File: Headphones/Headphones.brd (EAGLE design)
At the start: 50 x 50 mm, 3 parts, among them U1 SI4468

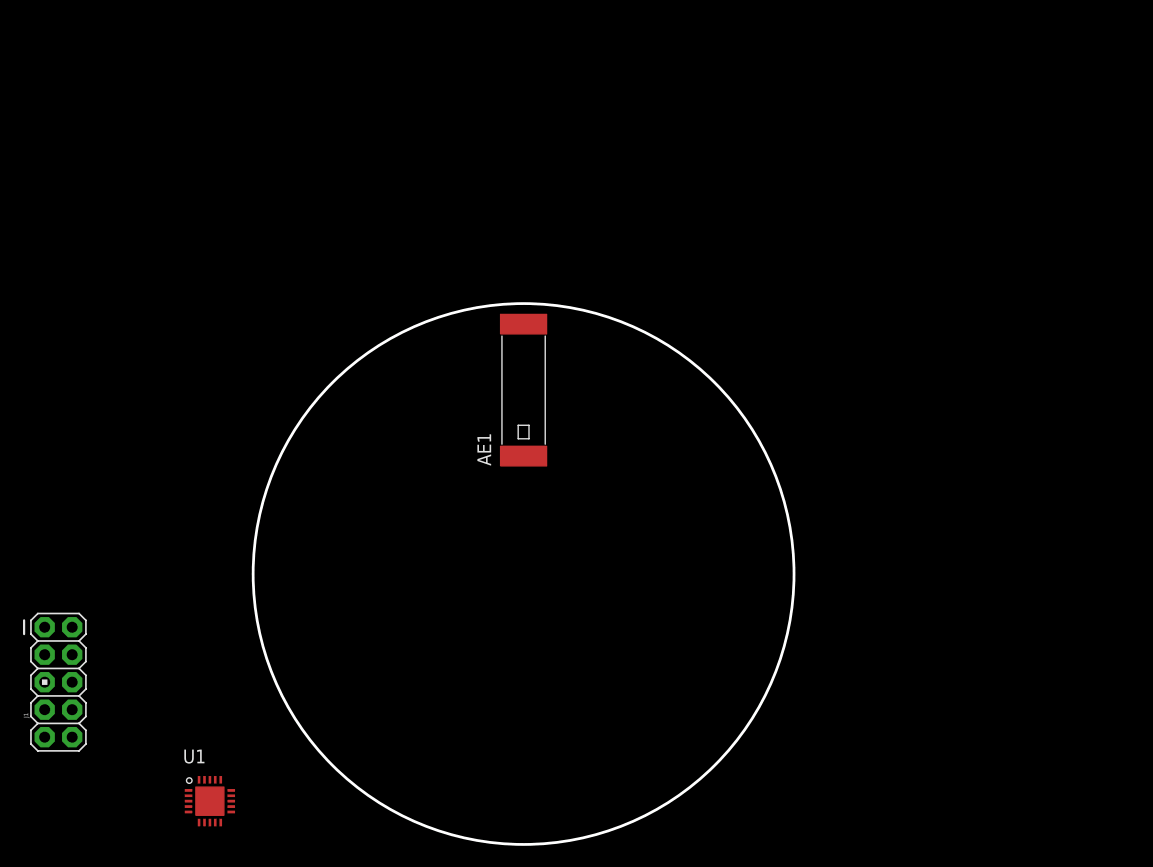
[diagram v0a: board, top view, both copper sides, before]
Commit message: Component placement is mostly complete. Need to finish routing
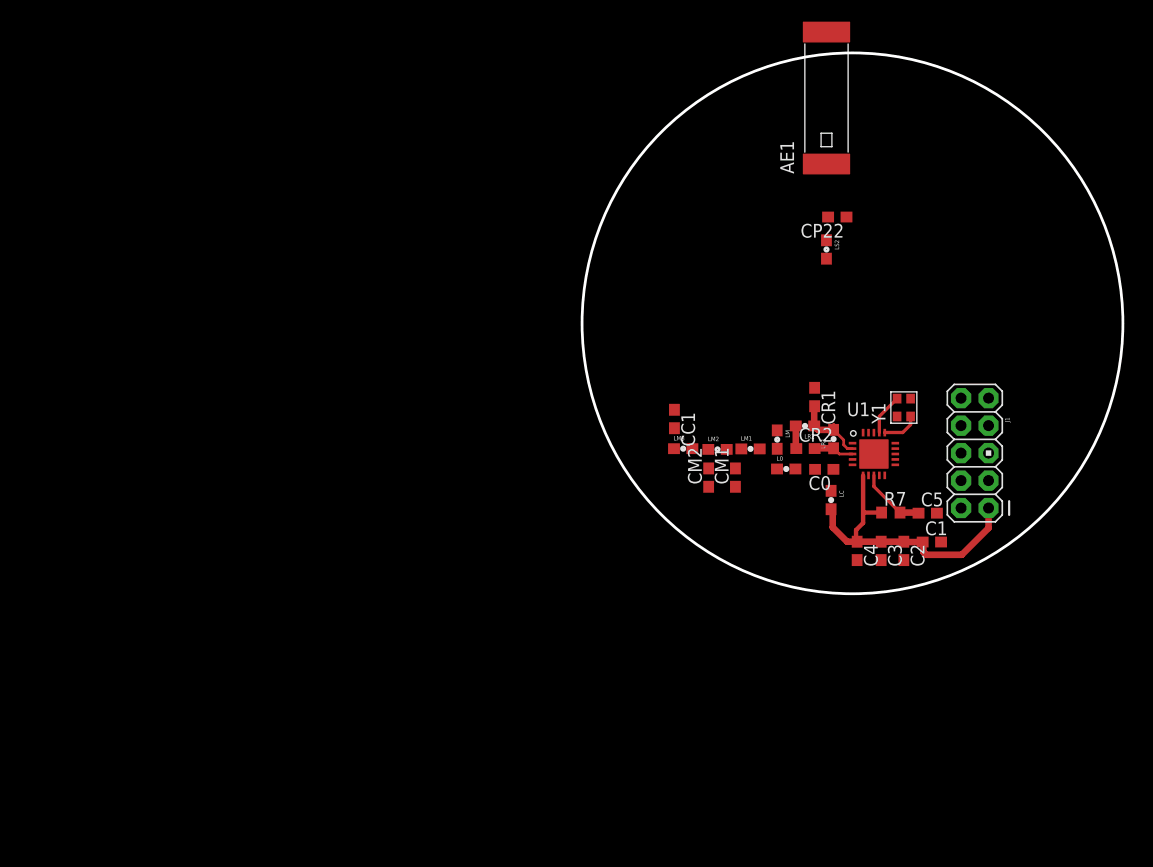
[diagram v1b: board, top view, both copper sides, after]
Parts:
- added C0, CM1, CM2: 4.7pF, resistor:C0603
- added C1: 2.2uF, resistor:C0603
- added C2, C5: 100nF, resistor:C0603
- added C3: 100pF, resistor:C0603
- added C4: 220pF, resistor:C0603
- added CC1: 56pF, resistor:C0603
- added CP22: 1.2pF, resistor:C0603
- added CR1: 3pF, resistor:C0603
- added CR2: 1pF, resistor:C0603
- added L0: 3.3nH, SparkFun-Passives:0603
- added LC: 100nH, SparkFun-Passives:0603
- added LM: 6.2nH, SparkFun-Passives:0603
- added LM1, LM3: 6.8nH, SparkFun-Passives:0603
- added LM2: 13nH, SparkFun-Passives:0603
- added LR1: 18nH, SparkFun-Passives:0603
- added LR2: 22nH, SparkFun-Passives:0603
- added LS2: 10nH, SparkFun-Passives:0603
- added R7: 4.7, resistor:R0603
- added Y1: 30MHz, Master:ABM10
- moved J1 87.3 mm to (41.7, 11.2), turned to 180 degrees
- moved U1 69.3 mm to (32.4, 11.1)
- moved AE1 38.9 mm to (28.0, 44.0)
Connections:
- new net GPIO0: J1.5, U1.9
- new net GPIO1: J1.7, U1.10
- new net N$1: U1.16, Y1.1
- new net N$10: C0.1, LC.1, U1.4
- new net N$11: CM1.2, LM1.1, LM2.2
- new net N$12: CM2.2, LM2.1, LM3.2
- new net N$13: AE1.1, CP22.2, LS2.1
- new net N$2: U1.17, Y1.3
- new net N$3: C0.2, L0.2
- new net N$4: CR2.2, LR1.1, U1.3
- new net N$5: CR1.2, LR1.2, LR2.1, U1.2
- new net N$6: CR2.1, L0.1, LM.2, LM1.2, LR2.2
- new net N$9: CC1.1, LS2.2
- net 3V3: now also C1.1, C2.1, C3.1, C4.1, LC.2, R7.1, U1.6
- net GND: now also C1.2, C2.2, C3.2, C4.2, C5.2, CM1.1, CM2.1, CP22.1, CR1.1, J1.9, LM.1, Y1.2, Y1.4
- net N$7: now also C5.1, R7.2
- net N$8: now also CC1.2, LM3.1; no longer U1.6
- net NIRQ: now also J1.2; no longer J1.10
- net NSEL: now also J1.10; no longer J1.2
- net SCLK: now also J1.4; no longer J1.8
- net SDI: now also J1.8; no longer J1.4
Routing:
- net 3V3: track 0.00 -> 28.8 mm
- net N$5: track 0.00 -> 7.27 mm
- net N$7: track 0.00 -> 6.17 mm
- net N$2: track 0.00 -> 3.82 mm
- net N$4: track 0.00 -> 3.74 mm
- net N$1: track 0.00 -> 3.45 mm
- net N$6: track 0.00 -> 2.11 mm

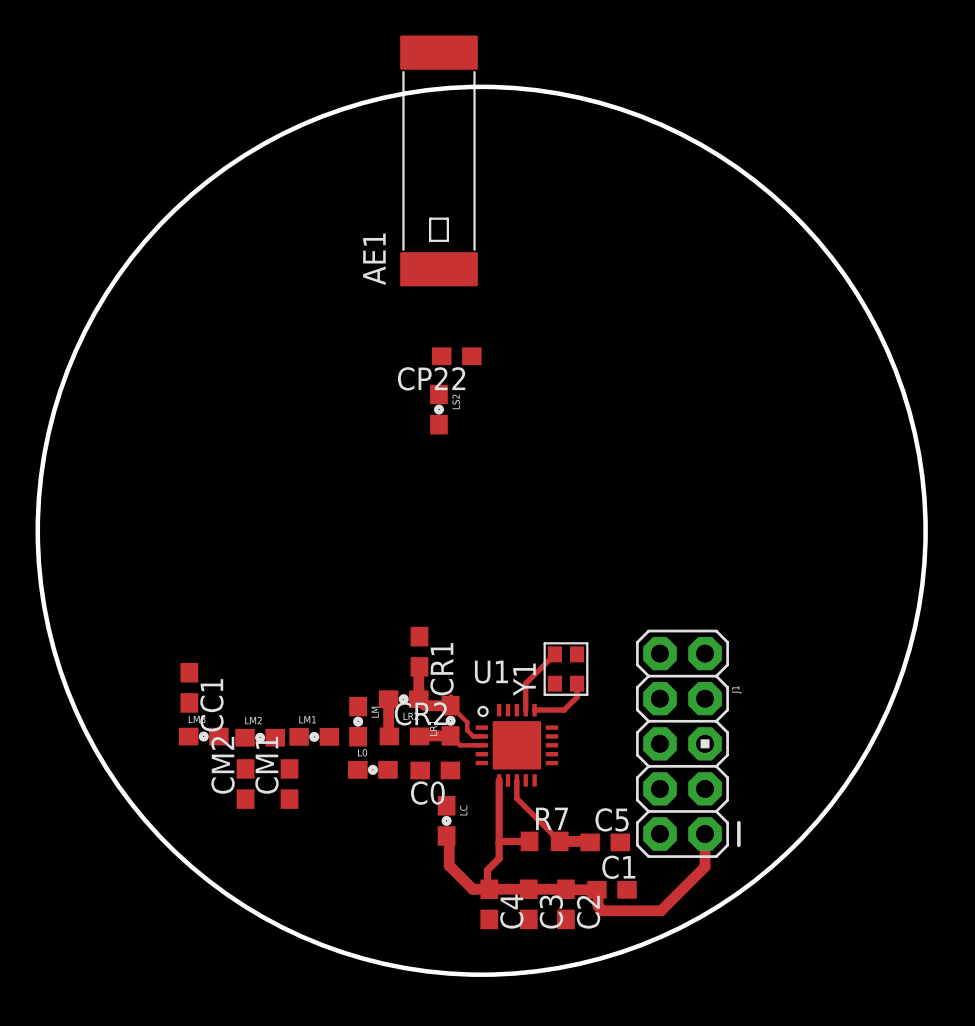
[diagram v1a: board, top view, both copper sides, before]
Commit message: Finished most of the layout. Still need to run DRC, ERC, and standardize text
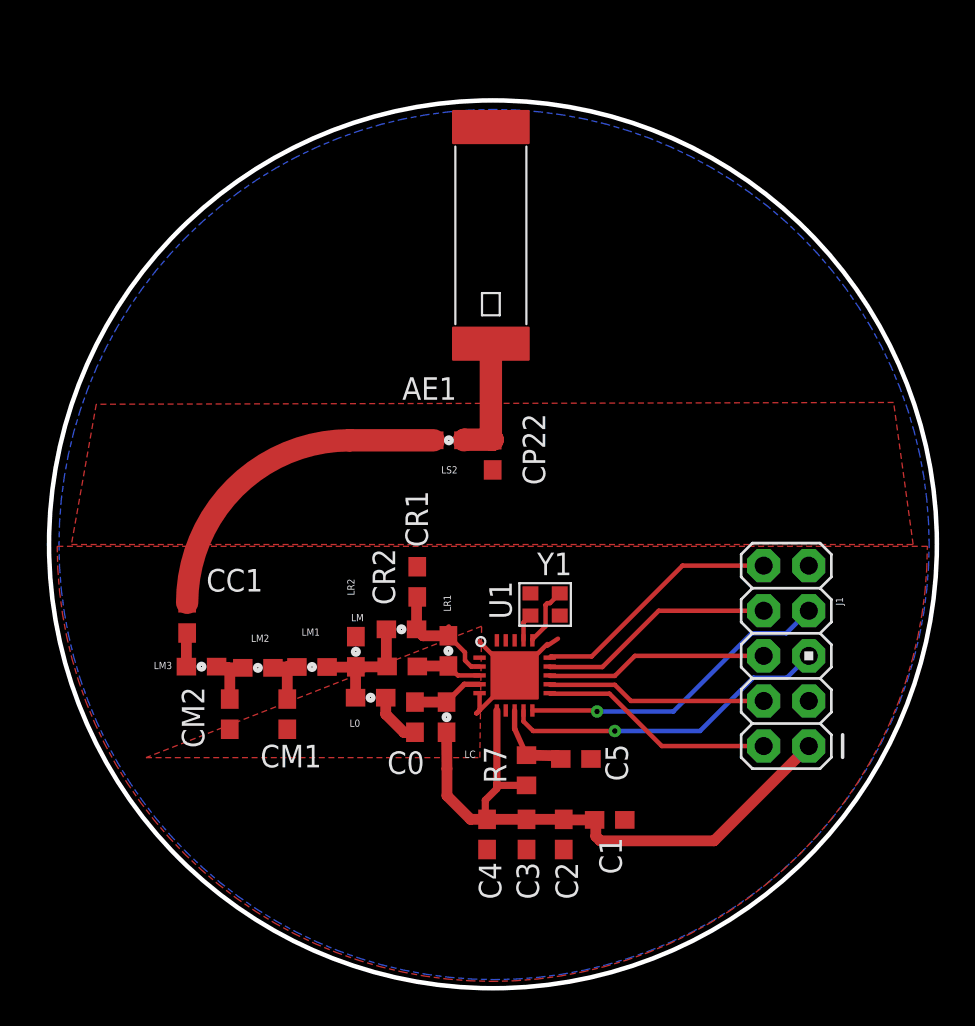
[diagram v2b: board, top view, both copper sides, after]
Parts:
- C2: value 100nF -> 220nF
- C4: value 220pF -> 100pF
- moved J1 7.66 mm to (47.6, 16.1)
- moved CP22 5.91 mm to (31.0, 27.5), turned to 90 degrees
- moved LC 5.84 mm to (28.4, 12.7)
- moved AE1 5.11 mm to (30.9, 39.8)
- moved C5 4.98 mm to (35.7, 10.3)
- moved R7 4.14 mm to (32.9, 9.69), turned to 90 degrees
- moved L0 4.07 mm to (24.2, 13.8)
- moved CM2 4.04 mm to (16.2, 12.8)
- moved CM1 3.94 mm to (19.5, 12.8)
- moved CR1 3.94 mm to (26.8, 20.3)
- moved CR2 3.94 mm to (25.9, 15.5)
- moved LR1 3.94 mm to (28.5, 16.4)
- moved LR2 3.94 mm to (25.9, 17.6)
- moved C2 3.94 mm to (35.0, 6.08)
- moved C3 3.94 mm to (32.9, 6.08)
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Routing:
- net GPIO0: track 0.00 -> 18.7 mm, vias 0 -> 1
- net GPIO1: track 0.00 -> 17.9 mm, vias 0 -> 1
- net N$9: track 0.00 -> 17.7 mm
- net NSEL: track 0.00 -> 14.2 mm
- net SDI: track 0.00 -> 13.4 mm
- net NIRQ: track 0.00 -> 13.3 mm
- net SDO: track 0.00 -> 12.5 mm
- net SCLK: track 0.00 -> 12.4 mm
- net GND: track 0.00 -> 7.33 mm
- net N$13: track 0.00 -> 7.18 mm
- net 3V3: track 28.8 -> 35.8 mm
- net N$6: track 2.11 -> 7.23 mm
- net N$10: track 0.00 -> 4.05 mm
- net N$12: track 0.00 -> 3.30 mm
- net N$11: track 0.00 -> 3.18 mm
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- added copper zone on layer 1, net GND
- added copper zone on layer 16, net GND

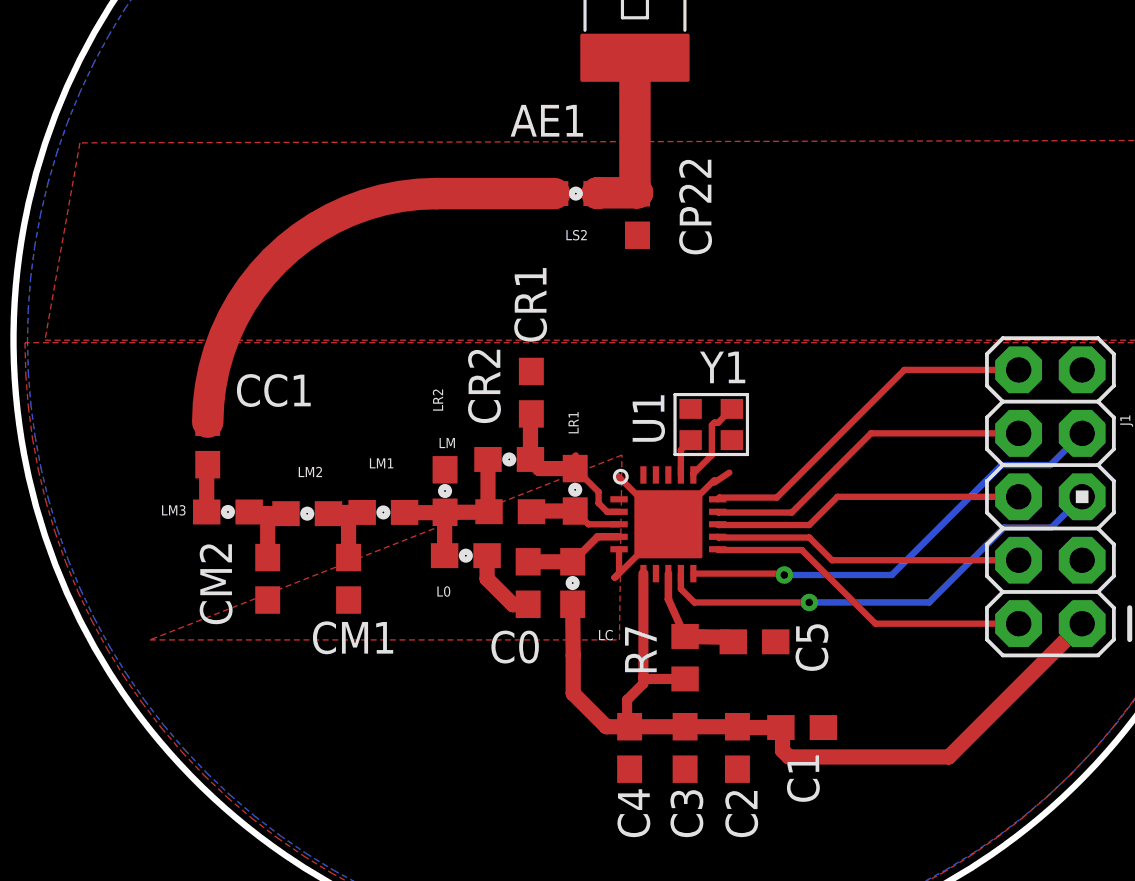
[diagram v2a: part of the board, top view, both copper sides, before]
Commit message: Added a bunch of vias everywhere
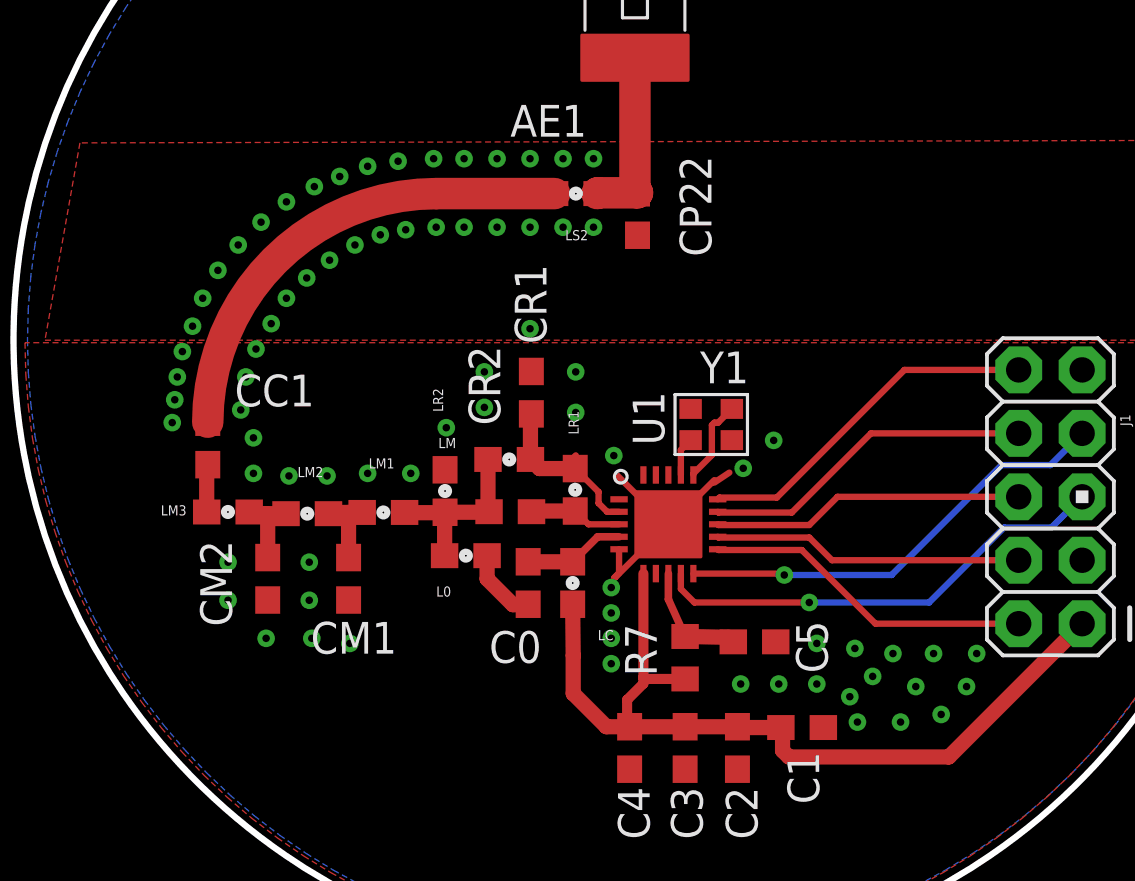
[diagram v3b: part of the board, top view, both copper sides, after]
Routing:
- net GND: vias 0 -> 77
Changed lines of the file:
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@@
 <setting verticaltext="up"/>
 </settings>
-<grid distance="0.0999999999" unitdist="mm" unit="mm" style="lines" multiple="1" display="yes" altdistance="0.025" altunitdist="inch" altunit="inch"/>
+<grid distance="4" unitdist="mil" unit="mil" style="lines" multiple="1" display="yes" altdistance="0.025" altunitdist="inch" altunit="inch"/>
 <layers>
 <layer number="1" name="Top" color="4" fill="1" visible="yes" active="yes"/>
@@
 <vertex x="6.6" y="22.4" curve="180"/>
 </polygon>
-<polygon width="0.3" layer="1" isolate="0.5">
-<vertex x="30.4" y="17.8"/>
-<vertex x="11.5" y="10.4"/>
-<vertex x="30.3" y="10.4"/>
-</polygon>
 <wire x1="32.259" y1="15.03" x2="30.129" y2="12.9" width="0.254" layer="1"/>
 <wire x1="30.129" y1="12.9" x2="30.1" y2="12.9" width="0.254" layer="1"/>
@@
 </polygon>
 <wire x1="34.1" y1="16.7" x2="34.7" y2="17.1" width="0.254" layer="1"/>
+<via x="15.1384" y="19.6088" extent="1-16" drill="0.3"/>
+<via x="15.3416" y="20.9296" extent="1-16" drill="0.3"/>
+<via x="15.748" y="22.0472" extent="1-16" drill="0.3"/>
+<via x="16.3576" y="23.0632" extent="1-16" drill="0.3"/>
+<via x="16.9672" y="24.0792" extent="1-16" drill="0.3"/>
 <wire x1="34.1" y1="16.7" x2="34.1" y2="16.8" width="0" layer="19" extent="1-1"/>
 <wire x1="32.259" y1="17.005" x2="33.3" y2="16.1" width="0" layer="19" extent="1-1"/>
 <wire x1="32.259" y1="15.03" x2="33.3" y2="16.1" width="0" layer="19" extent="1-1"/>
-<wire x1="36.558" y1="10.324" x2="32.259" y2="15.03" width="0" layer="19" extent="1-1"/>
-<wire x1="35.024" y1="5.225" x2="38.463" y2="6.893" width="0" layer="19" extent="1-1"/>
-<wire x1="31.023" y1="26.602" x2="26.774" y2="21.149" width="0" layer="19" extent="1-1"/>
+<wire x1="38.463" y1="6.893" x2="35.024" y2="5.225" width="0" layer="19" extent="1-1"/>
+<via x="17.78" y="24.892" extent="1-16" drill="0.3"/>
+<via x="18.6944" y="25.6032" extent="1-16" drill="0.3"/>
+<via x="19.7104" y="26.2128" extent="1-16" drill="0.3"/>
+<via x="20.7264" y="26.6192" extent="1-16" drill="0.3"/>
+<via x="21.7424" y="26.8224" extent="1-16" drill="0.3"/>
+<via x="22.9616" y="26.924" extent="1-16" drill="0.3"/>
+<via x="24.0792" y="26.924" extent="1-16" drill="0.3"/>
+<via x="25.4" y="26.924" extent="1-16" drill="0.3"/>
+<wire x1="25.6032" y1="26.924" x2="25.6032" y2="26.924" width="0" layer="19" extent="1-16"/>
+<wire x1="26.5176" y1="26.924" x2="26.5176" y2="26.924" width="0" layer="19" extent="1-16"/>
+<via x="29.972" y="12.4968" extent="1-16" drill="0.3"/>
+<via x="29.972" y="11.4808" extent="1-16" drill="0.3"/>
+<via x="29.972" y="10.4648" extent="1-16" drill="0.3"/>
+<via x="29.972" y="9.4488" extent="1-16" drill="0.3"/>
+<via x="26.7208" y="26.924" extent="1-16" drill="0.3"/>
+<via x="28.0416" y="26.924" extent="1-16" drill="0.3"/>
+<via x="29.2608" y="26.924" extent="1-16" drill="0.3"/>
+<via x="29.2608" y="29.6672" extent="1-16" drill="0.3"/>
+<via x="28.0416" y="29.6672" extent="1-16" drill="0.3"/>
+<via x="26.7208" y="29.6672" extent="1-16" drill="0.3"/>
+<via x="25.4" y="29.6672" extent="1-16" drill="0.3"/>
+<via x="24.0792" y="29.6672" extent="1-16" drill="0.3"/>
+<via x="22.86" y="29.6672" extent="1-16" drill="0.3"/>
+<via x="21.4376" y="29.5656" extent="1-16" drill="0.3"/>
+<via x="20.2184" y="29.3624" extent="1-16" drill="0.3"/>
+<via x="19.1008" y="28.956" extent="1-16" drill="0.3"/>
+<via x="18.0848" y="28.5496" extent="1-16" drill="0.3"/>
+<via x="16.9672" y="27.94" extent="1-16" drill="0.3"/>
+<via x="15.9512" y="27.1272" extent="1-16" drill="0.3"/>
+<via x="15.0368" y="26.2128" extent="1-16" drill="0.3"/>
+<via x="14.224" y="25.1968" extent="1-16" drill="0.3"/>
+<via x="13.6144" y="24.0792" extent="1-16" drill="0.3"/>
+<via x="13.208" y="22.9616" extent="1-16" drill="0.3"/>
+<via x="12.8016" y="21.9456" extent="1-16" drill="0.3"/>
+<via x="12.5984" y="20.9296" extent="1-16" drill="0.3"/>
+<via x="12.4968" y="20.0152" extent="1-16" drill="0.3"/>
+<via x="12.3952" y="19.1008" extent="1-16" drill="0.3"/>
+<via x="35.2552" y="17.272" extent="1-16" drill="0.3"/>
+<via x="30.0736" y="17.78" extent="1-16" drill="0.3"/>
+<via x="35.1536" y="8.636" extent="1-16" drill="0.3"/>
+<via x="36.6776" y="8.636" extent="1-16" drill="0.3"/>
+<via x="28.5496" y="21.1328" extent="1-16" drill="0.3"/>
+<via x="28.5496" y="19.5072" extent="1-16" drill="0.3"/>
+<wire x1="28.5496" y1="18.9992" x2="28.5496" y2="18.9992" width="0" layer="19" extent="1-16"/>
+<via x="24.892" y="21.1328" extent="1-16" drill="0.3"/>
+<via x="24.892" y="19.7104" extent="1-16" drill="0.3"/>
+<via x="26.7208" y="22.86" extent="1-16" drill="0.3"/>
+<via x="23.368" y="18.8976" extent="1-16" drill="0.3"/>
+<via x="21.9456" y="17.0688" extent="1-16" drill="0.3"/>
+<via x="20.2184" y="17.0688" extent="1-16" drill="0.3"/>
+<via x="15.6464" y="17.0688" extent="1-16" drill="0.3"/>
+<via x="15.6464" y="18.4912" extent="1-16" drill="0.3"/>
+<via x="17.0688" y="16.9672" extent="1-16" drill="0.3"/>
+<via x="18.5928" y="16.9672" extent="1-16" drill="0.3"/>
+<via x="14.6304" y="13.5128" extent="1-16" drill="0.3"/>
+<via x="14.6304" y="11.9888" extent="1-16" drill="0.3"/>
+<via x="16.1544" y="10.4648" extent="1-16" drill="0.3"/>
+<via x="17.8816" y="13.5128" extent="1-16" drill="0.3"/>
+<via x="17.8816" y="11.9888" extent="1-16" drill="0.3"/>
+<via x="38.2016" y="10.2616" extent="1-16" drill="0.3"/>
+<via x="38.2016" y="8.636" extent="1-16" drill="0.3"/>
+<via x="39.5224" y="8.128" extent="1-16" drill="0.3"/>
+<via x="39.8272" y="7.112" extent="1-16" drill="0.3"/>
+<via x="41.5544" y="7.112" extent="1-16" drill="0.3"/>
+<via x="43.18" y="7.4168" extent="1-16" drill="0.3"/>
+<via x="44.196" y="8.5344" extent="1-16" drill="0.3"/>
+<via x="44.6024" y="9.8552" extent="1-16" drill="0.3"/>
+<via x="42.8752" y="9.8552" extent="1-16" drill="0.3"/>
+<via x="41.2496" y="9.8552" extent="1-16" drill="0.3"/>
+<via x="39.7256" y="10.0584" extent="1-16" drill="0.3"/>
+<via x="40.4368" y="8.9408" extent="1-16" drill="0.3"/>
+<via x="42.164" y="8.5344" extent="1-16" drill="0.3"/>
+<via x="36.4744" y="18.3896" extent="1-16" drill="0.3"/>
+<via x="19.5072" y="10.2616" extent="1-16" drill="0.3"/>
+<via x="17.9832" y="10.4648" extent="1-16" drill="0.3"/>
 </signal>
 <signal name="N$7">
